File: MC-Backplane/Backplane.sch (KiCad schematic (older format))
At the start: 1 part, among them J1 1730010

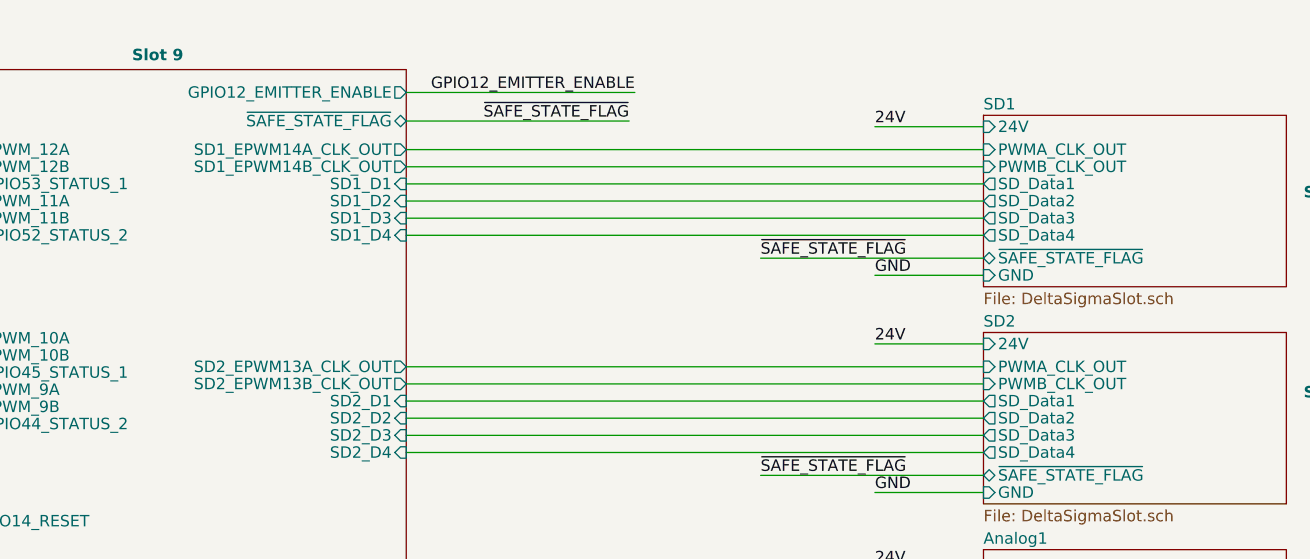
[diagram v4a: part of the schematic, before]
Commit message: spread tracks across available space
could still add some test points
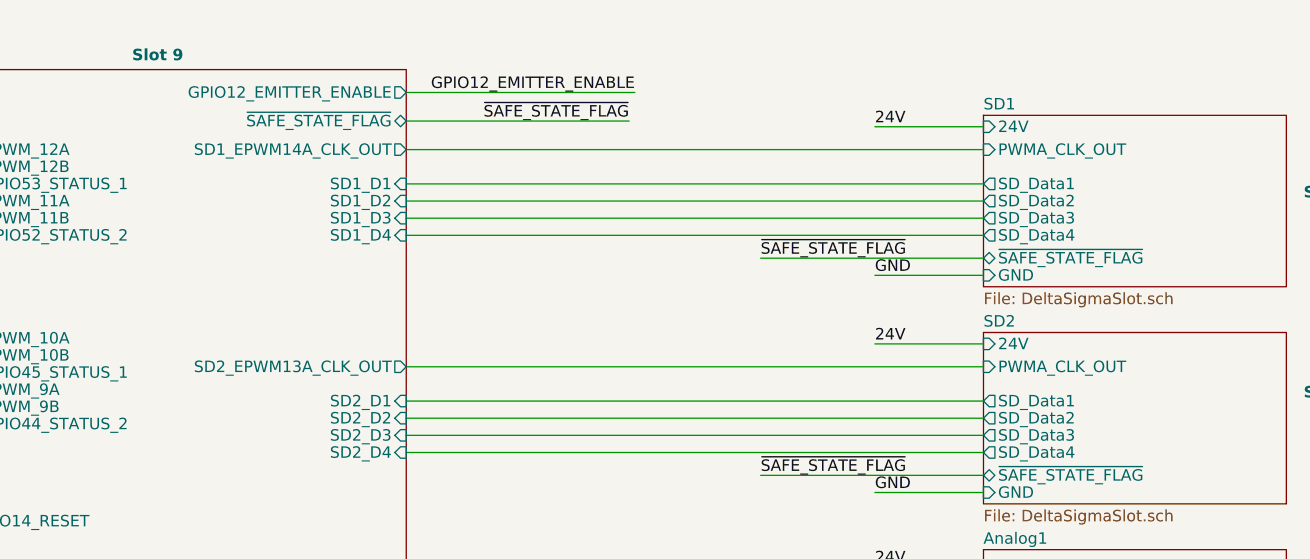
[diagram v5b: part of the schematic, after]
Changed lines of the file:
@@
 F3 "24V" I L 9200 950 50
 F4 "PWMA_CLK_OUT" I L 9200 1050 50
-F5 "PWMB_CLK_OUT" I L 9200 1125 50
-F6 "~SAFE_STATE_FLAG~" B L 9200 1525 50
-F7 "SD_Data2" O L 9200 1275 50
-F8 "SD_Data1" O L 9200 1200 50
-F9 "SD_Data4" O L 9200 1425 50
-F10 "SD_Data3" O L 9200 1350 50
+F5 "~SAFE_STATE_FLAG~" B L 9200 1525 50
+F6 "SD_Data2" O L 9200 1275 50
+F7 "SD_Data1" O L 9200 1200 50
+F8 "SD_Data4" O L 9200 1425 50
+F9 "SD_Data3" O L 9200 1350 50
 $EndSheet
 $Sheet
@@
 F3 "24V" I L 9200 1900 50
 F4 "PWMA_CLK_OUT" I L 9200 2000 50
-F5 "PWMB_CLK_OUT" I L 9200 2075 50
-F6 "~SAFE_STATE_FLAG~" B L 9200 2475 50
-F7 "SD_Data2" O L 9200 2225 50
-F8 "SD_Data1" O L 9200 2150 50
-F9 "SD_Data4" O L 9200 2375 50
-F10 "SD_Data3" O L 9200 2300 50
+F5 "~SAFE_STATE_FLAG~" B L 9200 2475 50
+F6 "SD_Data2" O L 9200 2225 50
+F7 "SD_Data1" O L 9200 2150 50
+F8 "SD_Data4" O L 9200 2375 50
+F9 "SD_Data3" O L 9200 2300 50
 $EndSheet
 $Sheet
@@
 Text Label 3025 1325 2    50   ~ 0
 ~SAFE_STATE_FLAG~
-Text Label 2525 1400 2    50   ~ 0
 Wire Wire Line
 	2050 1475 2525 1475
@@
 Text Label 3050 4850 2    50   ~ 0
 ~SAFE_STATE_FLAG~
-Text Label 2525 4925 2    50   ~ 0
 Wire Wire Line
 	2050 5000 2525 5000
-Text Label 2525 5000 2    50   ~ 0
-GND
 Wire Wire Line
 	2050 6025 3050 6025
 Text Label 3050 6025 2    50   ~ 0
 ~SAFE_STATE_FLAG~
-Text Label 2525 6100 2    50   ~ 0
 Wire Wire Line
 	2050 6175 2525 6175
@@
 Text Label 3050 7200 2    50   ~ 0
 ~SAFE_STATE_FLAG~
-Text Label 2525 7275 2    50   ~ 0
 Wire Wire Line
 	2050 7350 2525 7350
@@
 	9200 1050 6675 1050
 Wire Wire Line
-	9200 1125 6675 1125
-Wire Wire Line
 	9200 2000 6675 2000
-Wire Wire Line
-	9200 2075 6675 2075
 Wire Wire Line
 	9200 1525 8225 1525
@@
 F17 "ADC1_D3" O R 6675 3325 50
 F18 "SD2_EPWM13A_CLK_OUT" O R 6675 2000 50
-F19 "SD2_EPWM13B_CLK_OUT" O R 6675 2075 50
-F20 "GPIO12_EMITTER_ENABLE" O R 6675 800 50
-F21 "~SAFE_STATE_FLAG~" B R 6675 925 50
-F22 "GD1_EPWM_11A" O L 4575 1275 50
-F23 "GD1_EPWM_11B" O L 4575 1350 50
-F24 "GD1_GPIO53_STATUS_1" I L 4575 1200 50
-F25 "GD1_EPWM_12A" O L 4575 1050 50
-F26 "GD1_EPWM_12B" O L 4575 1125 50
-F27 "GD1_GPIO52_STATUS_2" I L 4575 1425 50
-F28 "GD2_EPWM_9A" O L 4575 2100 50
-F29 "GD2_EPWM_9B" O L 4575 2175 50
-F30 "GD2_GPIO44_STATUS_2" I L 4575 2250 50
-F31 "GD2_GPIO45_STATUS_1" I L 4575 2025 50
-F32 "GD3_EPWM_7A" O L 4575 3275 50
-F33 "GD3_EPWM_7B" O L 4575 3350 50
-F34 "GD3_GPIO25_STATUS_1" I L 4575 3200 50
-F35 "GD3_EPWM_8A" O L 4575 3050 50
-F36 "GD3_EPWM_8B" O L 4575 3125 50
-F37 "GD3_GPIO24_STATUS_2" I L 4575 3425 50
-F38 "SD1_EPWM14A_CLK_OUT" O R 6675 1050 50
-F39 "SD1_EPWM14B_CLK_OUT" O R 6675 1125 50
-F40 "GD_EPWM_5A" O L 4575 4450 50
-F41 "GD_EPWM_5B" O L 4575 4525 50
-F42 "GD4_GPIO23_STATUS_1" I L 4575 4375 50
-F43 "GD_EPWM_6A" O L 4575 4225 50
-F44 "GD_EPWM_6B" O L 4575 4300 50
-F45 "GD4_GPIO22_STATUS_2" I L 4575 4600 50
-F46 "GD5_GPIO18_STATUS_2" I L 4575 5150 50
-F47 "GD5_EPWM_4B" O L 4575 4850 50
-F48 "GD5_EPWM_4A" O L 4575 4775 50
-F49 "GD5_GPIO19_STATUS_1" I L 4575 4925 50
-F50 "GD5_EPWM_3B" O L 4575 5075 50
-F51 "GD5_EPWM_3A" O L 4575 5000 50
-F52 "GD6_GPIO15_STATUS_2" I L 4575 5725 50
-F53 "GD6_EPWM_2B" O L 4575 5425 50
-F54 "GD6_EPWM_2A" O L 4575 5350 50
-F55 "GD6_GPIO16_STATUS_1" I L 4575 5500 50
-F56 "GD6_EPWM_1B" O L 4575 5650 50
-F57 "GD6_EPWM_1A" O L 4575 5575 50
-F58 "GD_GPIO14_RESET" O L 4575 2675 50
-F59 "GD2_EPWM_10A" O L 4575 1875 50
-F60 "GD2_EPWM_10B" O L 4575 1950 50
-F61 "ADC2_D0" O R 6675 4325 50
-F62 "ADC2_D1" O R 6675 4400 50
-F63 "ADC1_14" O R 6675 2950 50
-F64 "ADC1_15" O R 6675 3025 50
-F65 "SD1_D1" I R 6675 1200 50
-F66 "SD1_D4" I R 6675 1425 50
-F67 "SD1_D3" I R 6675 1350 50
-F68 "SD1_D2" I R 6675 1275 50
-F69 "SD2_D1" I R 6675 2150 50
-F70 "SD2_D4" I R 6675 2375 50
-F71 "SD2_D3" I R 6675 2300 50
-F72 "SD2_D2" I R 6675 2225 50
-$EndSheet
+F19 "GPIO12_EMITTER_ENABLE" O R 6675 800 50
+F20 "~SAFE_STATE_FLAG~" B R 6675 925 50
+F21 "GD1_EPWM_11A" O L 4575 1275 50
+F22 "GD1_EPWM_11B" O L 4575 1350 50
+F23 "GD1_GPIO53_STATUS_1" I L 4575 1200 50
+F24 "GD1_EPWM_12A" O L 4575 1050 50
+F25 "GD1_EPWM_12B" O L 4575 1125 50
+F26 "GD1_GPIO52_STATUS_2" I L 4575 1425 50
+F27 "GD2_EPWM_9A" O L 4575 2100 50
+F28 "GD2_EPWM_9B" O L 4575 2175 50
+F29 "GD2_GPIO44_STATUS_2" I L 4575 2250 50
+F30 "GD2_GPIO45_STATUS_1" I L 4575 2025 50
+F31 "GD3_EPWM_7A" O L 4575 3275 50
+F32 "GD3_EPWM_7B" O L 4575 3350 50
+F33 "GD3_GPIO25_STATUS_1" I L 4575 3200 50
+F34 "GD3_EPWM_8A" O L 4575 3050 50
+F35 "GD3_EPWM_8B" O L 4575 3125 50
+F36 "GD3_GPIO24_STATUS_2" I L 4575 3425 50
+F37 "SD1_EPWM14A_CLK_OUT" O R 6675 1050 50
+F38 "GD_EPWM_5A" O L 4575 4450 50
+F39 "GD_EPWM_5B" O L 4575 4525 50
+F40 "GD4_GPIO23_STATUS_1" I L 4575 4375 50
+F41 "GD_EPWM_6A" O L 4575 4225 50
+F42 "GD_EPWM_6B" O L 4575 4300 50
+F43 "GD4_GPIO22_STATUS_2" I L 4575 4600 50
+F44 "GD5_GPIO18_STATUS_2" I L 4575 5150 50
+F45 "GD5_EPWM_4B" O L 4575 4850 50
+F46 "GD5_EPWM_4A" O L 4575 4775 50
+F47 "GD5_GPIO19_STATUS_1" I L 4575 4925 50
+F48 "GD5_EPWM_3B" O L 4575 5075 50
+F49 "GD5_EPWM_3A" O L 4575 5000 50
+F50 "GD6_GPIO15_STATUS_2" I L 4575 5725 50
+F51 "GD6_EPWM_2B" O L 4575 5425 50
+F52 "GD6_EPWM_2A" O L 4575 5350 50
+F53 "GD6_GPIO16_STATUS_1" I L 4575 5500 50
+F54 "GD6_EPWM_1B" O L 4575 5650 50
+F55 "GD6_EPWM_1A" O L 4575 5575 50
+F56 "GD_GPIO14_RESET" O L 4575 2675 50
+F57 "GD2_EPWM_10A" O L 4575 1875 50
+F58 "GD2_EPWM_10B" O L 4575 1950 50
+F59 "ADC2_D0" O R 6675 4325 50
+F60 "ADC2_D1" O R 6675 4400 50
+F61 "ADC1_14" O R 6675 2950 50
+F62 "ADC1_15" O R 6675 3025 50
+F63 "SD1_D1" I R 6675 1200 50
+F64 "SD1_D4" I R 6675 1425 50
+F65 "SD1_D3" I R 6675 1350 50
+F66 "SD1_D2" I R 6675 1275 50
+F67 "SD2_D1" I R 6675 2150 50
+F68 "SD2_D4" I R 6675 2375 50
+F69 "SD2_D3" I R 6675 2300 50
+F70 "SD2_D2" I R 6675 2225 50
+$EndSheet
+Text Label 2525 5000 2    50   ~ 0
+GND
 $EndSCHEMATC

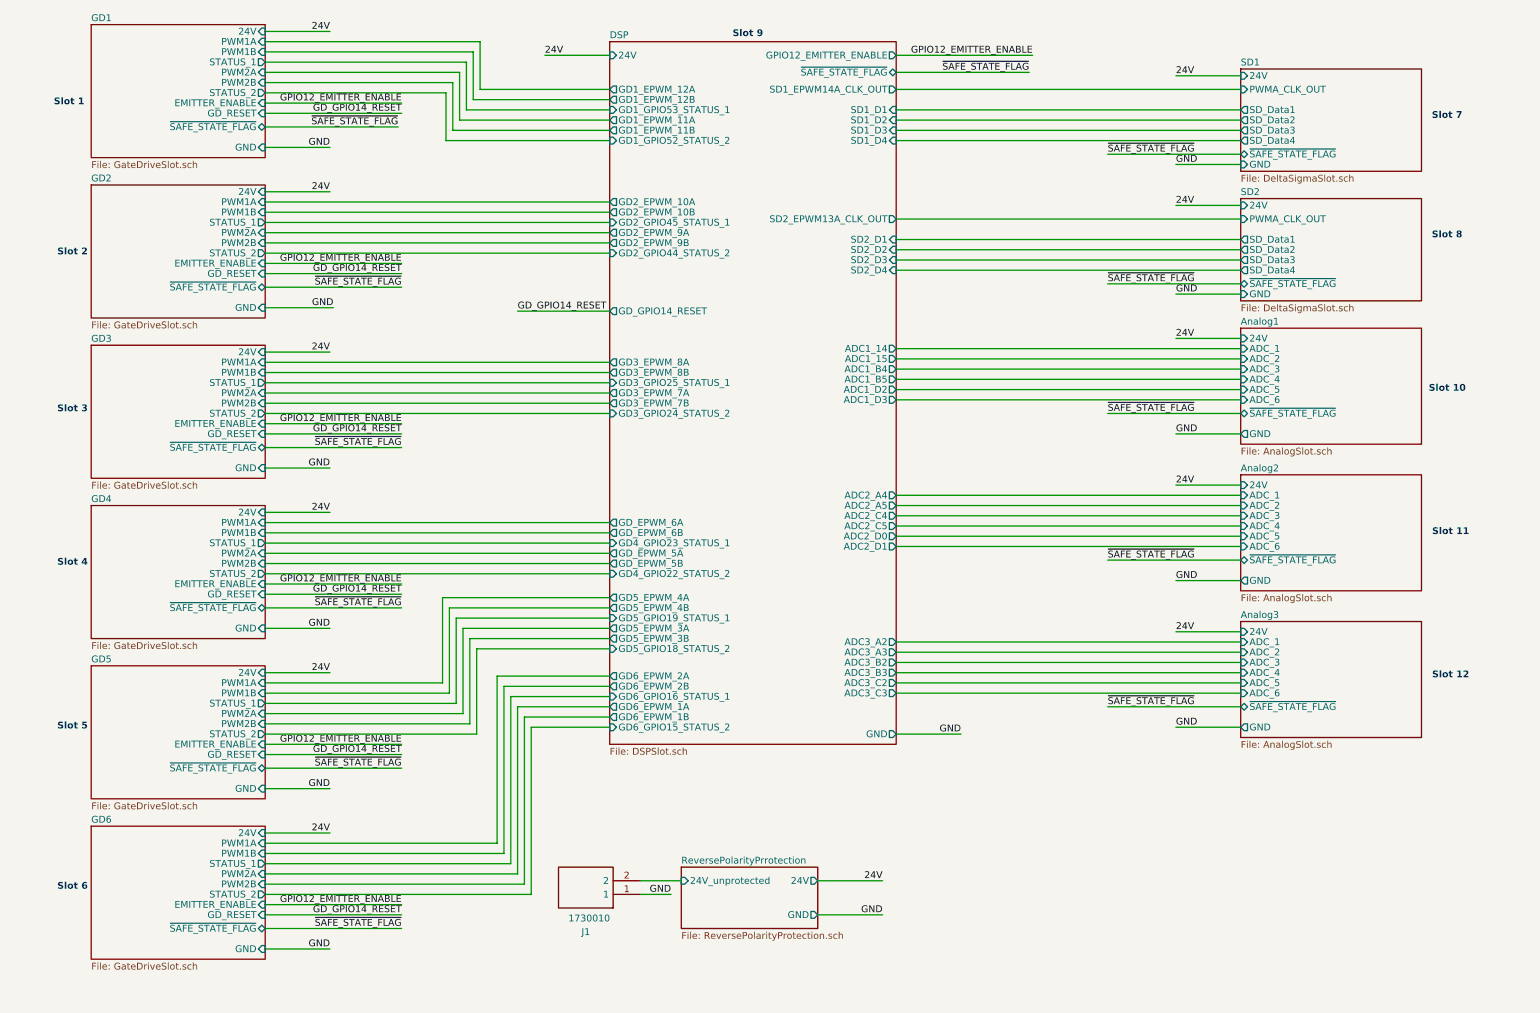
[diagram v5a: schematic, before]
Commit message: added testpoints
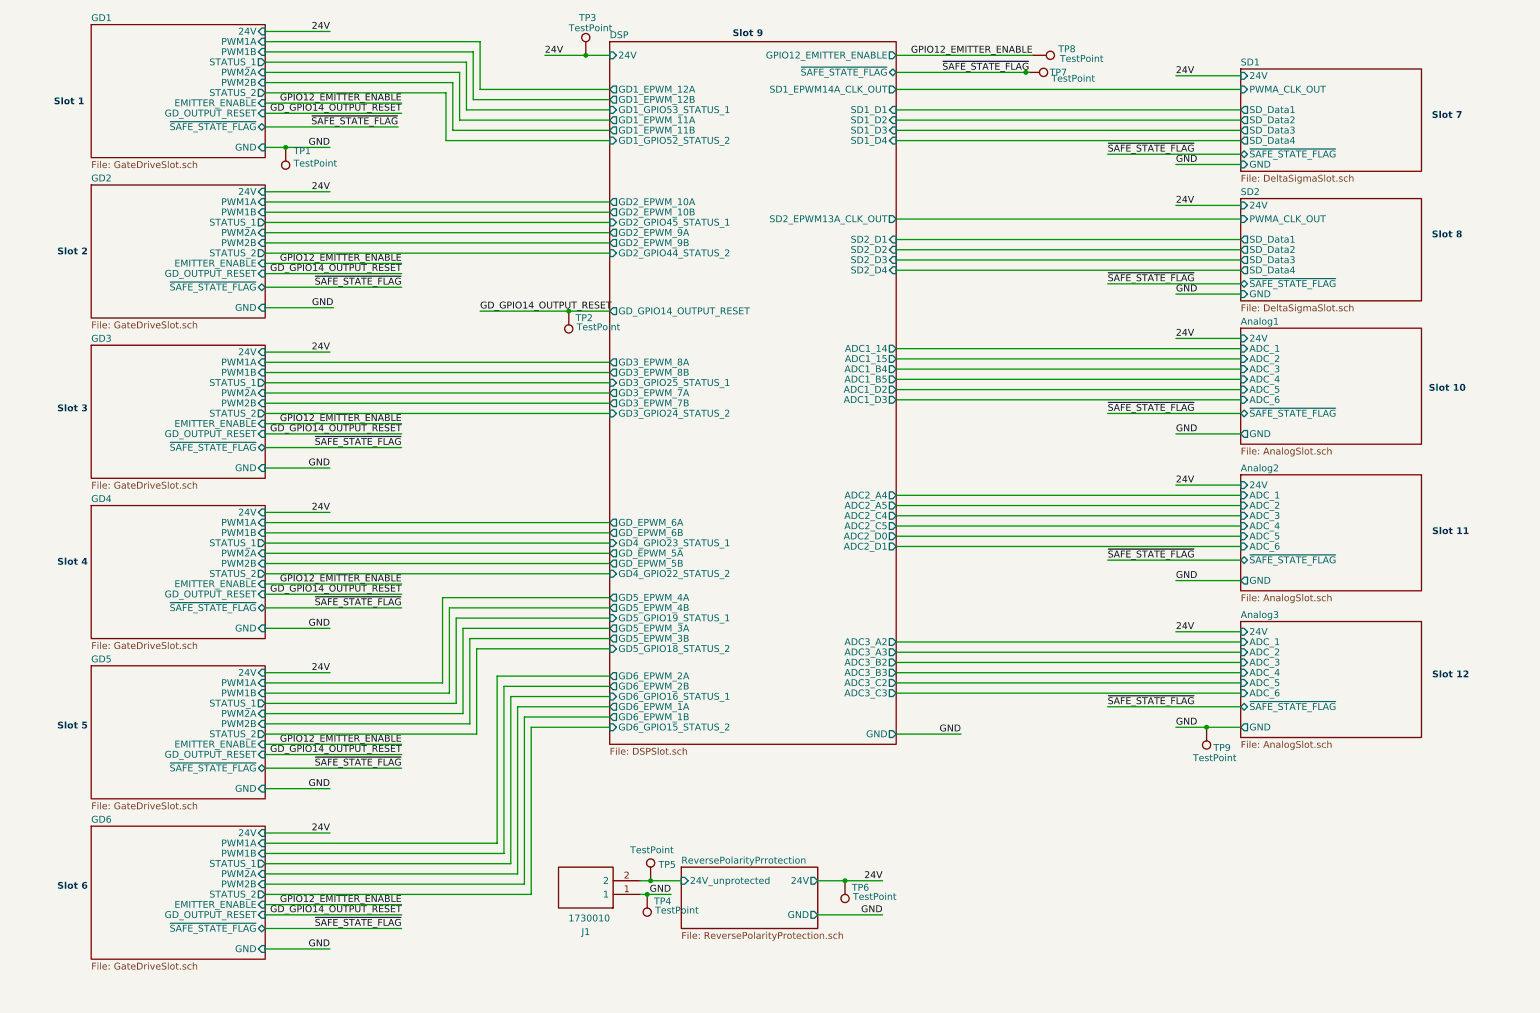
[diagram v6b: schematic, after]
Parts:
- added TP1, TP2, TP3, TP4, TP5, TP6, TP7, TP8, TP9: TestPoint, TestPoint:TestPoint_Plated_Hole_D2.0mm, symbol Connector:TestPoint
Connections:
- net 24V: now also TP3.1, TP6.1
- net GND: now also TP1.1, TP4.1, TP9.1
- net GPIO12_EMITTER_ENABLE: now also TP8.1
- net ReversePolarityPrrotection/24V_unprotected: now also TP5.1
- net ~SAFE_STATE_FLAG~: now also TP7.1
- new net GD_GPIO14_OUTPUT_RESET: TP2.1
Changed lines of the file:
@@
 $EndSheet
 Wire Wire Line
-	4800 6850 5100 6850
+	4800 6850 4875 6850
 $Sheet
 S 9200 900  1325 750
@@
 F1 "GateDriveSlot.sch" 50
 F2 "GND" I R 2050 1475 50
-F3 "GD_RESET" I R 2050 1225 50
+F3 "GD_OUTPUT_RESET" I R 2050 1225 50
 F4 "24V" I R 2050 625 50
 F5 "EMITTER_ENABLE" I R 2050 1150 50
@@
 F1 "GateDriveSlot.sch" 50
 F2 "GND" I R 2050 5000 50
-F3 "GD_RESET" I R 2050 4750 50
+F3 "GD_OUTPUT_RESET" I R 2050 4750 50
 F4 "24V" I R 2050 4150 50
 F5 "EMITTER_ENABLE" I R 2050 4675 50
@@
 F1 "GateDriveSlot.sch" 50
 F2 "GND" I R 2050 7350 50
-F3 "GD_RESET" I R 2050 7100 50
+F3 "GD_OUTPUT_RESET" I R 2050 7100 50
 F4 "24V" I R 2050 6500 50
 F5 "EMITTER_ENABLE" I R 2050 7025 50
@@
 F1 "GateDriveSlot.sch" 50
 F2 "GND" I R 2050 6175 50
-F3 "GD_RESET" I R 2050 5925 50
+F3 "GD_OUTPUT_RESET" I R 2050 5925 50
 F4 "24V" I R 2050 5325 50
 F5 "EMITTER_ENABLE" I R 2050 5850 50
@@
 GPIO12_EMITTER_ENABLE
 Text Label 3050 1225 2    50   ~ 0
-GD_GPIO14_RESET
+GD_GPIO14_OUTPUT_RESET
 Wire Wire Line
 	2050 2325 3050 2325
@@
 GPIO12_EMITTER_ENABLE
 Text Label 3050 2400 2    50   ~ 0
-GD_GPIO14_RESET
+GD_GPIO14_OUTPUT_RESET
 Wire Wire Line
 	2050 3500 3050 3500
@@
 GPIO12_EMITTER_ENABLE
 Text Label 3050 3575 2    50   ~ 0
-GD_GPIO14_RESET
+GD_GPIO14_OUTPUT_RESET
 Wire Wire Line
 	2050 4675 3050 4675
@@
 GPIO12_EMITTER_ENABLE
 Text Label 3050 4750 2    50   ~ 0
-GD_GPIO14_RESET
+GD_GPIO14_OUTPUT_RESET
 Wire Wire Line
 	2050 5850 3050 5850
@@
 GPIO12_EMITTER_ENABLE
 Text Label 3050 5925 2    50   ~ 0
-GD_GPIO14_RESET
+GD_GPIO14_OUTPUT_RESET
 Wire Wire Line
 	2050 7025 3050 7025
@@
 GPIO12_EMITTER_ENABLE
 Text Label 3050 7100 2    50   ~ 0
-GD_GPIO14_RESET
+GD_GPIO14_OUTPUT_RESET
 Wire Wire Line
 	2050 625  2525 625
@@
 ~SAFE_STATE_FLAG~
 Wire Wire Line
-	2050 1475 2525 1475
+	2050 1475 2200 1475
 Text Label 2525 1475 2    50   ~ 0
 GND
@@
 Text Label 2525 7350 2    50   ~ 0
 GND
-Text Label 3900 2675 0    50   ~ 0
-GD_GPIO14_RESET
-Wire Wire Line
-	4575 2675 3900 2675
+Text Label 3625 2675 0    50   ~ 0
+GD_GPIO14_OUTPUT_RESET
+Wire Wire Line
+	4575 2675 4275 2675
 Wire Wire Line
 	2050 5400 3350 5400
@@
 GND
 Wire Wire Line
-	9200 5725 8725 5725
+	9200 5725 8950 5725
 Text Label 8725 4650 0    50   ~ 0
 GND
@@
 ~SAFE_STATE_FLAG~
 Wire Wire Line
-	6675 925  7650 925
+	6675 925  7625 925
 Text Label 7650 925  2    50   ~ 0
 ~SAFE_STATE_FLAG~
@@
 GPIO12_EMITTER_ENABLE
 Wire Wire Line
-	4575 800  4100 800
+	4575 800  4400 800
 Text Label 4100 800  0    50   ~ 0
 24V
@@
 24V
 Wire Wire Line
-	6100 6850 6575 6850
+	6100 6850 6300 6850
 Text Label 6575 6850 2    50   ~ 0
 24V
@@
 GND
 Wire Wire Line
-	4800 6950 5025 6950
+	4800 6950 4850 6950
 Text Notes 725  1175 2    50   ~ 10
 Slot 1
@@
 F1 "GateDriveSlot.sch" 50
 F2 "GND" I R 2050 2650 50
-F3 "GD_RESET" I R 2050 2400 50
+F3 "GD_OUTPUT_RESET" I R 2050 2400 50
 F4 "24V" I R 2050 1800 50
 F5 "EMITTER_ENABLE" I R 2050 2325 50
@@
 F1 "GateDriveSlot.sch" 50
 F2 "GND" I R 2050 3825 50
-F3 "GD_RESET" I R 2050 3575 50
+F3 "GD_OUTPUT_RESET" I R 2050 3575 50
 F4 "24V" I R 2050 2975 50
 F5 "EMITTER_ENABLE" I R 2050 3500 50
@@
 F54 "GD6_EPWM_1B" O L 4575 5650 50
 F55 "GD6_EPWM_1A" O L 4575 5575 50
-F56 "GD_GPIO14_RESET" O L 4575 2675 50
+F56 "GD_GPIO14_OUTPUT_RESET" O L 4575 2675 50
 F57 "GD2_EPWM_10A" O L 4575 1875 50
 F58 "GD2_EPWM_10B" O L 4575 1950 50
@@
 Text Label 2525 5000 2    50   ~ 0
 GND
+$Comp
+L Connector:TestPoint TP1
+U 1 1 62328061
+P 2200 1475
+F 0 "TP1" H 2142 1501 50  0000 R CNN
+F 1 "TestPoint" H 2142 1592 50  0000 R CNN
+F 2 "TestPoint:TestPoint_Plated_Hole_D2.0mm" H 2400 1475 50  0001 C CNN
+F 3 "~" H 2400 1475 50  0001 C CNN
+	1    2200 1475
+	-1   0    0    1
+$EndComp
+Connection ~ 2200 1475
+Wire Wire Line
+	2200 1475 2525 1475
+$Comp
+L Connector:TestPoint TP2
+U 1 1 62328780
+P 4275 2675
+F 0 "TP2" H 4225 2725 50  0000 R CNN
+F 1 "TestPoint" H 4217 2792 50  0000 R CNN
+F 2 "TestPoint:TestPoint_Plated_Hole_D2.0mm" H 4475 2675 50  0001 C CNN
+F 3 "~" H 4475 2675 50  0001 C CNN
+	1    4275 2675
+	-1   0    0    1
+$EndComp
+Connection ~ 4275 2675
+Wire Wire Line
+	4275 2675 3625 2675
+$Comp
+L Connector:TestPoint TP7
+U 1 1 62329610
+P 7625 925
+F 0 "TP7" V 7625 1100 50  0000 L CNN
+F 1 "TestPoint" V 7670 1113 50  0000 L CNN
+F 2 "TestPoint:TestPoint_Plated_Hole_D2.0mm" H 7825 925 50  0001 C CNN
+F 3 "~" H 7825 925 50  0001 C CNN
+	1    7625 925
+	0    1    1    0
+$EndComp
+Connection ~ 7625 925
+Wire Wire Line
+	7625 925  7650 925
+$Comp
+L Connector:TestPoint TP8
+U 1 1 6232BBED
+P 7675 800
+F 0 "TP8" V 7629 988 50  0000 L CNN
+F 1 "TestPoint" V 7700 1000 50  0000 L CNN
+F 2 "TestPoint:TestPoint_Plated_Hole_D2.0mm" H 7875 800 50  0001 C CNN
+F 3 "~" H 7875 800 50  0001 C CNN
+	1    7675 800
+	0    1    1    0
+$EndComp
+$Comp
+L Connector:TestPoint TP3
+U 1 1 6232C061
+P 4400 800
+F 0 "TP3" H 4350 1075 50  0000 L CNN
+F 1 "TestPoint" H 4275 1000 50  0000 L CNN
+F 2 "TestPoint:TestPoint_Plated_Hole_D2.0mm" H 4600 800 50  0001 C CNN
+F 3 "~" H 4600 800 50  0001 C CNN
+	1    4400 800
+	1    0    0    -1
+$EndComp
+Connection ~ 4400 800
+Wire Wire Line
+	4400 800  4100 800
+$Comp
+L Connector:TestPoint TP4
+U 1 1 62337FB9
+P 4850 6950
+F 0 "TP4" H 4800 7000 50  0000 R CNN
+F 1 "TestPoint" H 4792 7067 50  0000 R CNN
+F 2 "TestPoint:TestPoint_Plated_Hole_D2.0mm" H 5050 6950 50  0001 C CNN
+F 3 "~" H 5050 6950 50  0001 C CNN
+	1    4850 6950
+	-1   0    0    1
+$EndComp
+Connection ~ 4850 6950
+Wire Wire Line
+	4850 6950 5025 6950
+$Comp
+L Connector:TestPoint TP5
+U 1 1 6233880B
+P 4875 6850
+F 0 "TP5" H 4933 6968 50  0000 L CNN
+F 1 "TestPoint" H 4725 7075 50  0000 L CNN
+F 2 "TestPoint:TestPoint_Plated_Hole_D2.0mm" H 5075 6850 50  0001 C CNN
+F 3 "~" H 5075 6850 50  0001 C CNN
+	1    4875 6850
+	1    0    0    -1
+$EndComp
+Connection ~ 4875 6850
+Wire Wire Line
+	4875 6850 5100 6850
+$Comp
+L Connector:TestPoint TP6
+U 1 1 62338AF4
+P 6300 6850
+F 0 "TP6" H 6250 6900 50  0000 R CNN
+F 1 "TestPoint" H 6242 6967 50  0000 R CNN
+F 2 "TestPoint:TestPoint_Plated_Hole_D2.0mm" H 6500 6850 50  0001 C CNN
+F 3 "~" H 6500 6850 50  0001 C CNN
+	1    6300 6850
+	-1   0    0    1
+$EndComp
+Connection ~ 6300 6850
+Wire Wire Line
+	6300 6850 6575 6850
+$Comp
+L Connector:TestPoint TP9
+U 1 1 623390BB
+P 8950 5725
+F 0 "TP9" H 8900 5875 50  0000 R CNN
+F 1 "TestPoint" H 9050 5950 50  0000 R CNN
+F 2 "TestPoint:TestPoint_Plated_Hole_D2.0mm" H 9150 5725 50  0001 C CNN
+F 3 "~" H 9150 5725 50  0001 C CNN
+	1    8950 5725
+	-1   0    0    1
+$EndComp
+Connection ~ 8950 5725
+Wire Wire Line
+	8950 5725 8725 5725
 $EndSCHEMATC
